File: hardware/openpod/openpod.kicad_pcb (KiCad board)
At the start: 2 copper layers, 42.8 x 59.9 mm, 14 parts, among them J1 SJ-43515TS-SMT-TR

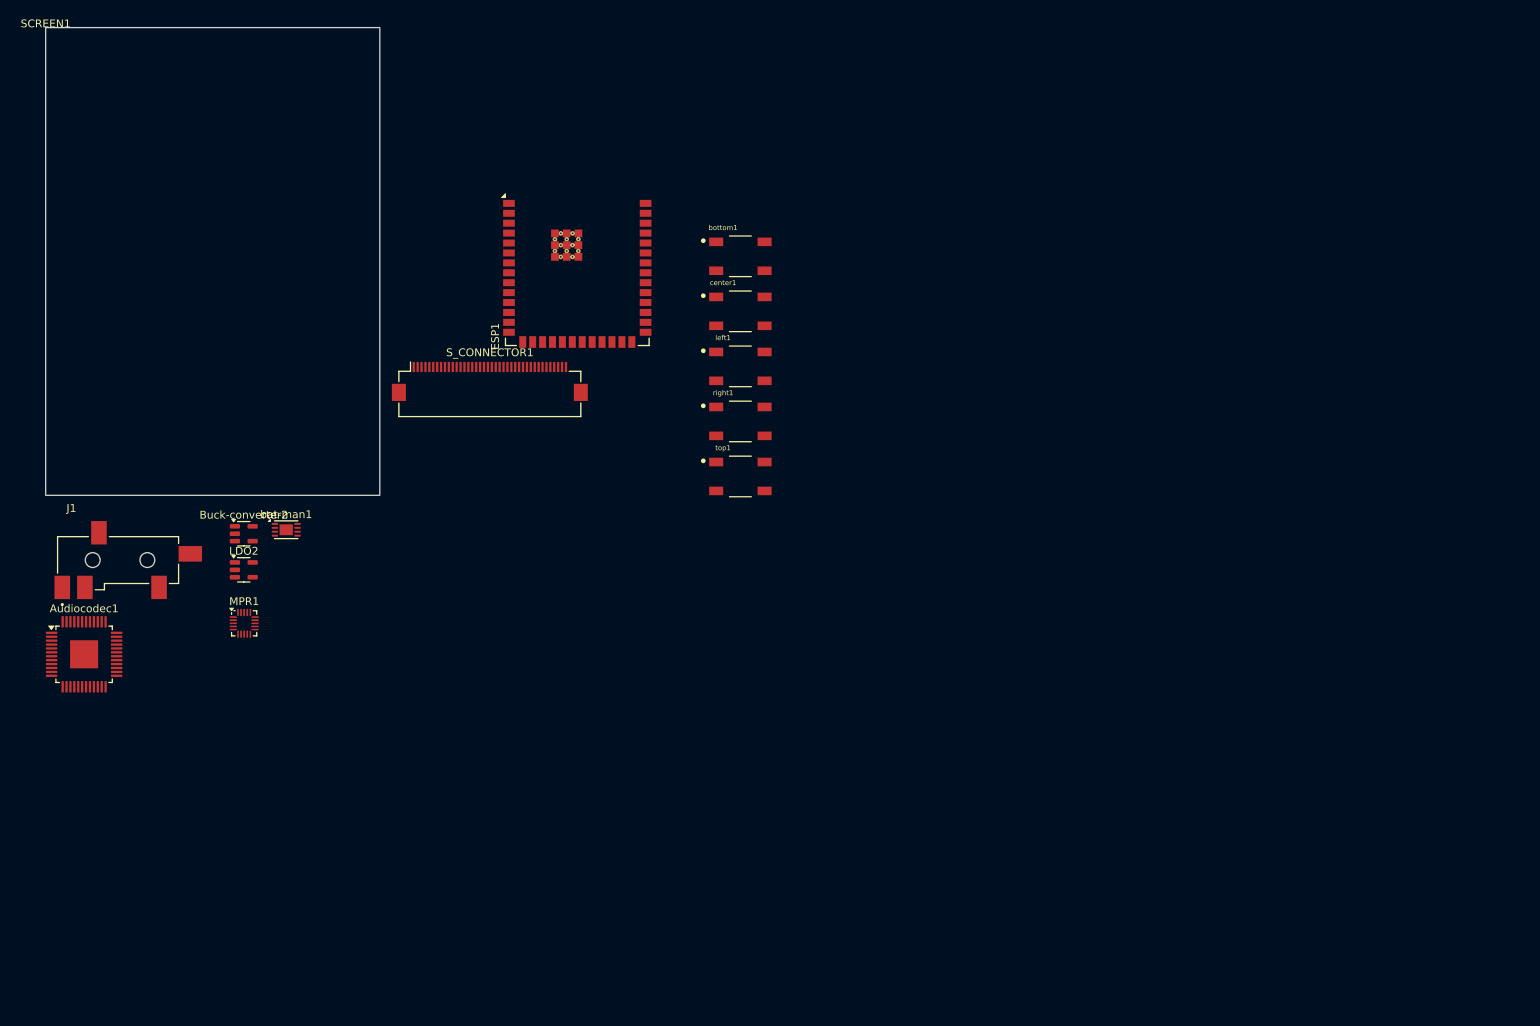
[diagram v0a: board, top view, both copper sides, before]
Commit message: Rebirth (#2)
* designed clickwheel and see if mpr121 can fit on it

* update power and audio

* added UART converter

* added bluetooth

* try up with vs1053 feather

* setupt the player file

* fill screen with different colors

* almost works with GFX, just wrong coordinates

* test MADCTL 1

* wrong, screen is all white

* screen pins before remap

* new pinout with consecutive 16bits on the PCs pins

* screen works

* added demo

* updated platformio.ini

* added blog

* cleanup

* first menu

* Fast (ugly) menu renderer

* ugly theme + blog post

* transition using HW scrolling

* breakdown ui

* 30 rows buffer

* remove row/col shit

* added content for the blog

* start restoring render of the now playing

* scroll to nowplaying

* working transitiontotracklist (but slight prolbem with last line)

* fixed the wrapping issue at the bottom

* update theme

* rewired vs1053

* screen and mp3 working

* pins

* updated mp3 pinout to have i2c available

* testing the clickwheel with teleplot: looking good !

* Debugging the wheel: it follows my finger on the screen

* first scrolling the tracks with the wheel !

* WIP

* use an app state and allow to use more bits per pixel

* setup unit tests

* std

* remove select track

* use doctest and reporter

* make tests pass

* cleanup

* fixed scripts

* faster render fonts

* dark background

* better state + events handler system

* wip

* faster renderer of tracklist + animations + better split between concerns

* 2 bits per pixel

* docs

* remove unit tests

* simplify ui list

* rename track to element

* rename track to element

* psram controller

* psram works on SPI1

* psram controller works

* indexer

* crawler

* radix tree?

* update trie generator

* started implementing storage

* trie index

* search works on the stm32

* can retrieve now paths

* sound player on the way

* enhanced mp3 working, but not flac

* flac plugin

* config files

* load flac plugin correctly: saccaded sound

* cleaning up

*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
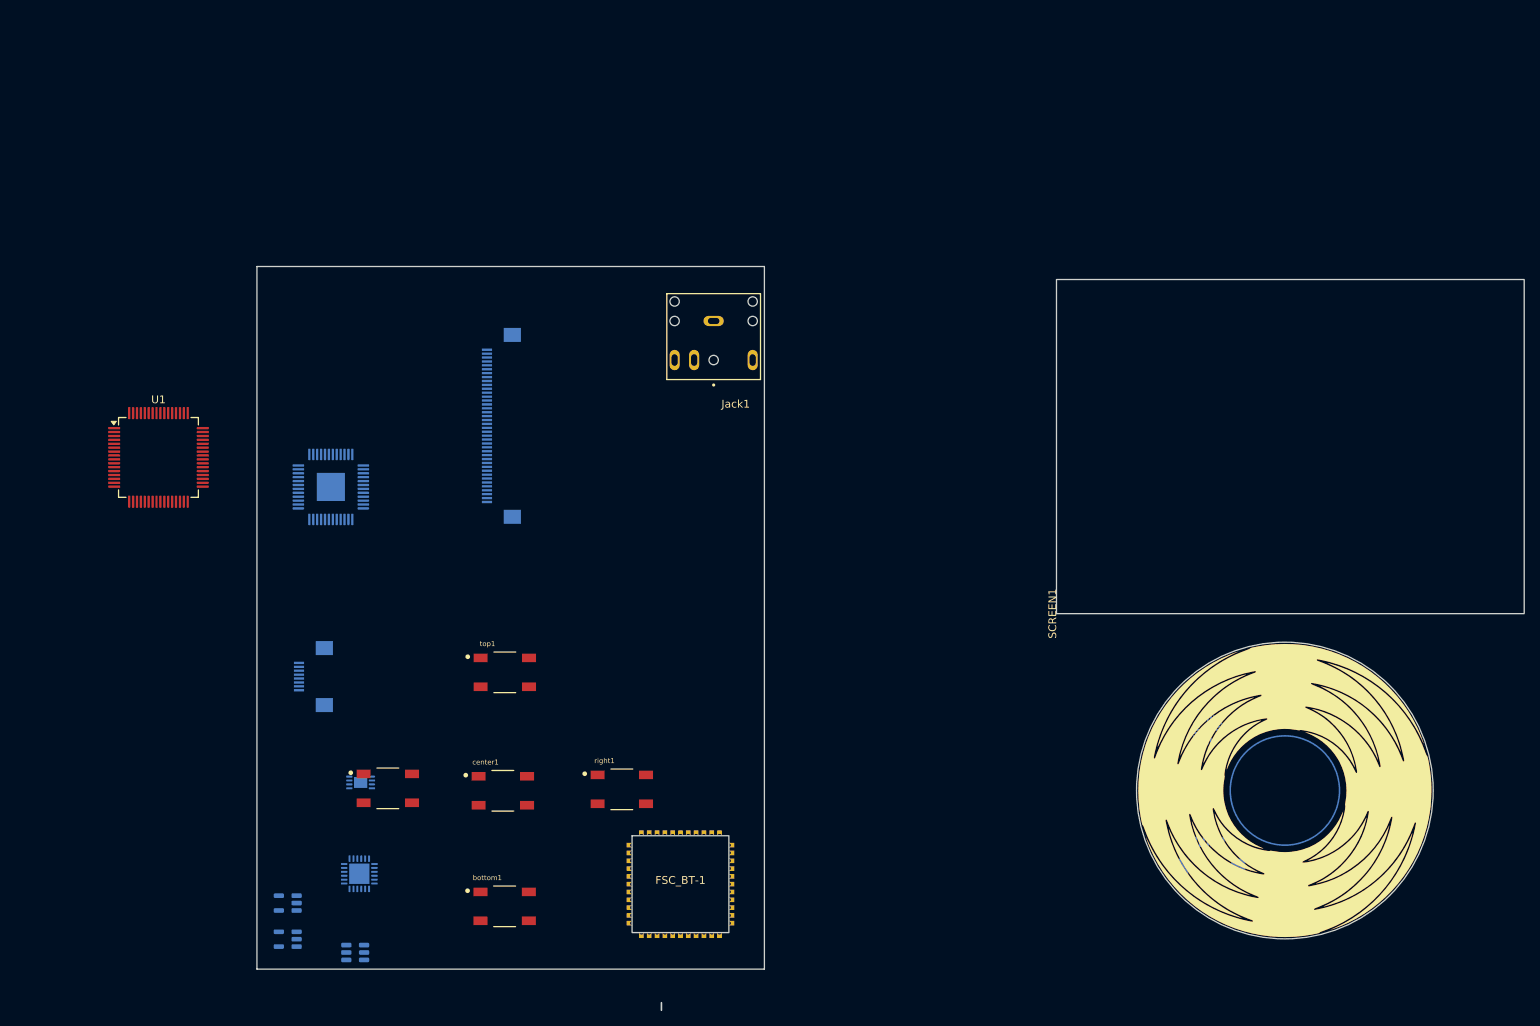
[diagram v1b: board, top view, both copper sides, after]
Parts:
- removed ESP1: ESP32-S3-WROOM-2, openpod:ESP32-S3-WROOM-2
- removed J1: SJ-43515TS-SMT-TR, jack:CUI_SJ-43515TS-SMT-TR
- added AP7312: ~, Package_TO_SOT_SMD:SOT-23-6, B.Cu at (112.7, 137.9)
- added Clickwheel1: ~, openpod:clickwheel_1, F.Cu at (231.7, 117.1)
- added FSC_BT-1: ~, openpod:fsc-bt1046, F.Cu at (154.3, 129.1)
- added Jack1: SJ1-3524NG, openpod:CUI_SJ1-3524NG, F.Cu at (158.6, 57.0)
- added U1: STM32F446RCTx, Package_QFP:LQFP-64_10x10mm_P0.5mm, F.Cu at (87.5, 74.5)
- added UART_BRIDGE1: CP2102N-Axx-xQFN24, Package_DFN_QFN:QFN-24-1EP_4x4mm_P0.5mm_EP2.6x2.6mm, B.Cu at (113.2, 127.8)
- added clickwheel-connector1: ~, Connector_FFC-FPC:Hirose_FH12-8S-0.5SH_1x08-1MP_P0.50mm_Horizontal, B.Cu at (222.1, 125.5)
- added clickwheel-connector2: ~, Connector_FFC-FPC:Hirose_FH12-8S-0.5SH_1x08-1MP_P0.50mm_Horizontal, B.Cu at (107.3, 102.5)
- Audiocodec1, Buck-converter2, LDO2, S_CONNECTOR1, bat-man1: moved to B.Cu
- MPR1: footprint Package_DFN_QFN:UQFN-20_3x3mm_P0.4mm -> openpod:mpr121qr2; moved to B.Cu
- moved SCREEN1 149.7 mm to (202.5, 94.5), turned to 90 degrees
- moved MPR1 124.2 mm to (221.9, 109.3), turned to 90 degrees
- moved bottom1 88.6 mm to (131.8, 132.0)
- moved left1 70.4 mm to (116.8, 116.8)
- moved center1 68.5 mm to (131.6, 117.1)
- moved right1 49.5 mm to (146.8, 117.0)
- moved Buck-converter2 47.6 mm to (104.0, 131.5), turned to 180 degrees
- moved LDO2 47.6 mm to (104.0, 136.2), turned to 180 degrees
- moved top1 39.2 mm to (131.8, 102.0)
- moved Audiocodec1 38.2 mm to (109.5, 78.2), turned to 180 degrees
- moved bat-man1 33.7 mm to (113.4, 116.1), turned to 180 degrees
- moved S_CONNECTOR1 5.88 mm to (131.4, 70.4), turned to -90 degrees
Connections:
- net Net-(BT2-+) renamed VBAT
- Buck-converter2 pad 3: 3.3V -> Net-(Buck-converter2-EN)
- Buck-converter2 pad 4: 3.3V -> Net-(Buck-converter2-EN)
- MPR1 pad 1: unconnected-(MPR1-~{IRQ}-Pad1) -> Net-(MPR1-~{IRQ})
- MPR1 pad 15: unconnected-(MPR1-LED3/ELE7-Pad15) -> Net-(Clickwheel1-right)
- MPR1 pad 16: unconnected-(MPR1-LED4/ELE8-Pad16) -> Net-(Clickwheel1-top)
- MPR1 pad 19: unconnected-(MPR1-LED7/ELE11-Pad19) -> Net-(Clickwheel1-bottom)
- MPR1 pad 2: unconnected-(MPR1-SCL-Pad2) -> Net-(MPR1-SCL)
- MPR1 pad 20: unconnected-(MPR1-VDD-Pad20) -> Net-(MPR1-VDD)
- MPR1 pad 3: unconnected-(MPR1-SDA-Pad3) -> Net-(MPR1-SDA)
- MPR1 pad 4: unconnected-(MPR1-ADDR-Pad4) -> Net-(MPR1-ADDR)
- MPR1 pad 5: unconnected-(MPR1-VREG-Pad5) -> Net-(MPR1-VREG)
- MPR1 pad 6: unconnected-(MPR1-VSS-Pad6) -> Net-(MPR1-VSS)
- MPR1 pad 7: unconnected-(MPR1-REXT-Pad7) -> Net-(MPR1-REXT)
- MPR1 pad 9: unconnected-(MPR1-ELE1-Pad9) -> Net-(Clickwheel1-left)
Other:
- board size 42.8 x 59.9 mm -> 65 x 95.3 mm
